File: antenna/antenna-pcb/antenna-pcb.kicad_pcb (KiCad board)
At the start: 2 copper layers, 97 x 97 mm, 11 parts, among them J1 SMA Connector Male, U1 HHM1589D1

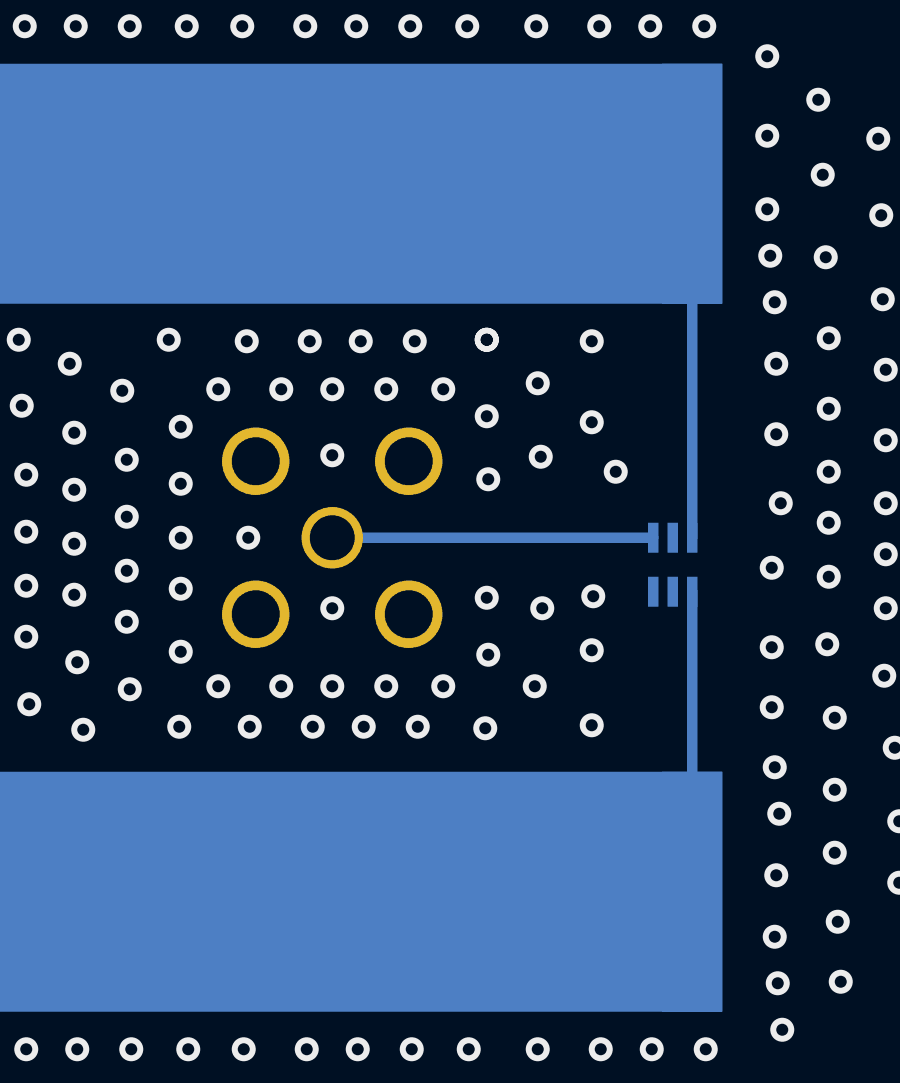
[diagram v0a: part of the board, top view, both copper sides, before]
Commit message: modify antenna pcbs and drc checked
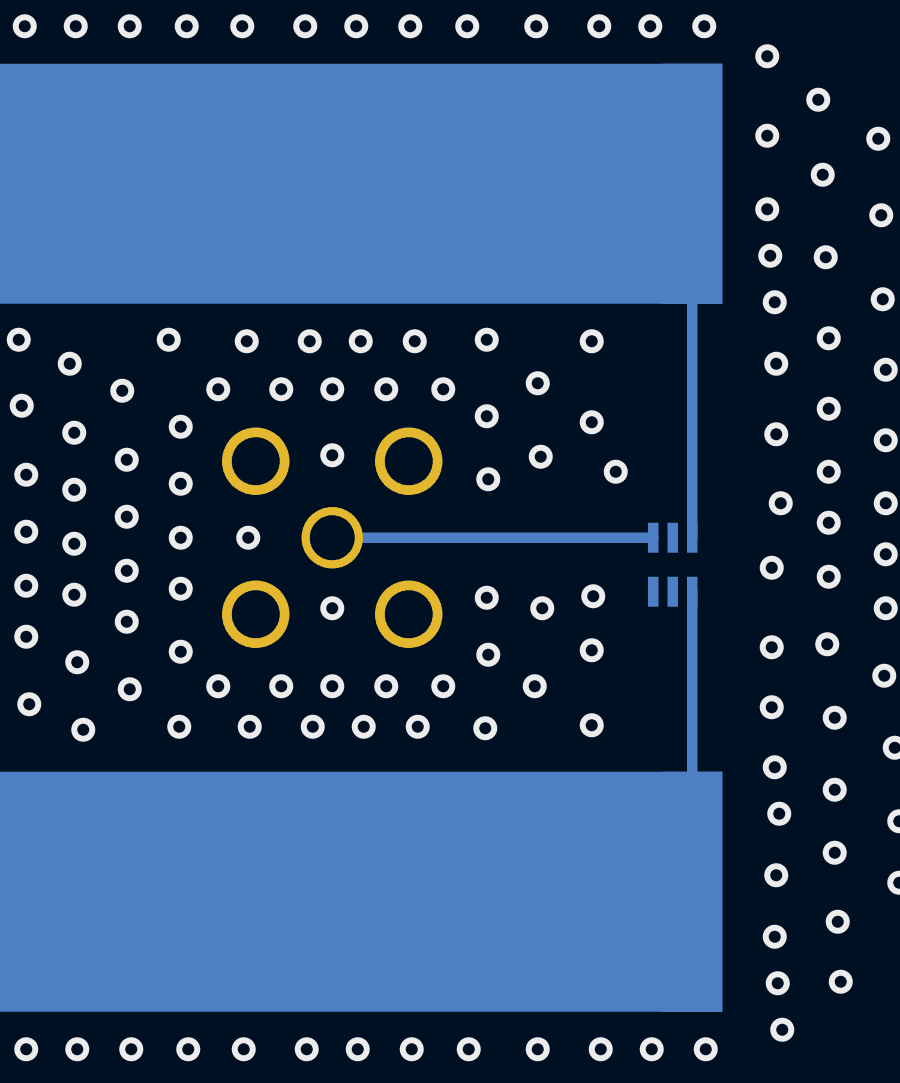
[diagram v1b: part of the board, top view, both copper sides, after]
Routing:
- net Net-(U1-Pad3): track 23.4 -> 11.8 mm
- net Net-(U1-Pad4): track 13.9 -> 10.0 mm
- net GND: vias 210 -> 209
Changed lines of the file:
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@@
   (via (at 108.05 91.9) (size 0.8) (drill 0.4) (layers "F.Cu" "B.Cu") (free) (net 3))
   (via (at 108.3 98.3) (size 0.8) (drill 0.4) (layers "F.Cu" "B.Cu") (free) (net 3))
-  (via (at 123.65 91.9) (size 0.8) (drill 0.4) (layers "F.Cu" "B.Cu") (free) (net 3))
   (via (at 103.85 86.45) (size 0.8) (drill 0.4) (layers "F.Cu" "B.Cu") (free) (net 3))
   (via (at 120.3 93.55) (size 0.8) (drill 0.4) (layers "F.Cu" "B.Cu") (free) (net 3))
@@
   (via (at 121.25 91.95) (size 0.8) (drill 0.4) (layers "F.Cu" "B.Cu") (free) (net 3))
   (segment (start 130.5 86.7) (end 130.5 98.5) (width 0.35) (layer "B.Cu") (net 4))
-  (segment (start 126.3 89.42) (end 123.58 86.7) (width 0.25) (layer "B.Cu") (net 4))
-  (segment (start 126.3 86.7) (end 118.5 86.7) (width 0.25) (layer "B.Cu") (net 4))
-  (segment (start 126.35 110.5) (end 126.3 110.55) (width 0.25) (layer "B.Cu") (net 5))
-  (segment (start 126.3 107.58) (end 123.58 110.3) (width 0.25) (layer "B.Cu") (net 5))
   (segment (start 130.5 100.3) (end 130.5 110.3) (width 0.35) (layer "B.Cu") (net 5))
   (zone (net 3) (net_name "GND") (layers F&B.Cu) (hatch edge 0.508)
